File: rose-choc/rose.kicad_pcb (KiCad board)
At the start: 2 copper layers, 145.2 x 97.3 mm, 67 parts, among them SW1 Switch, U1 Arduino_Pro_Micro, U2 TRRS

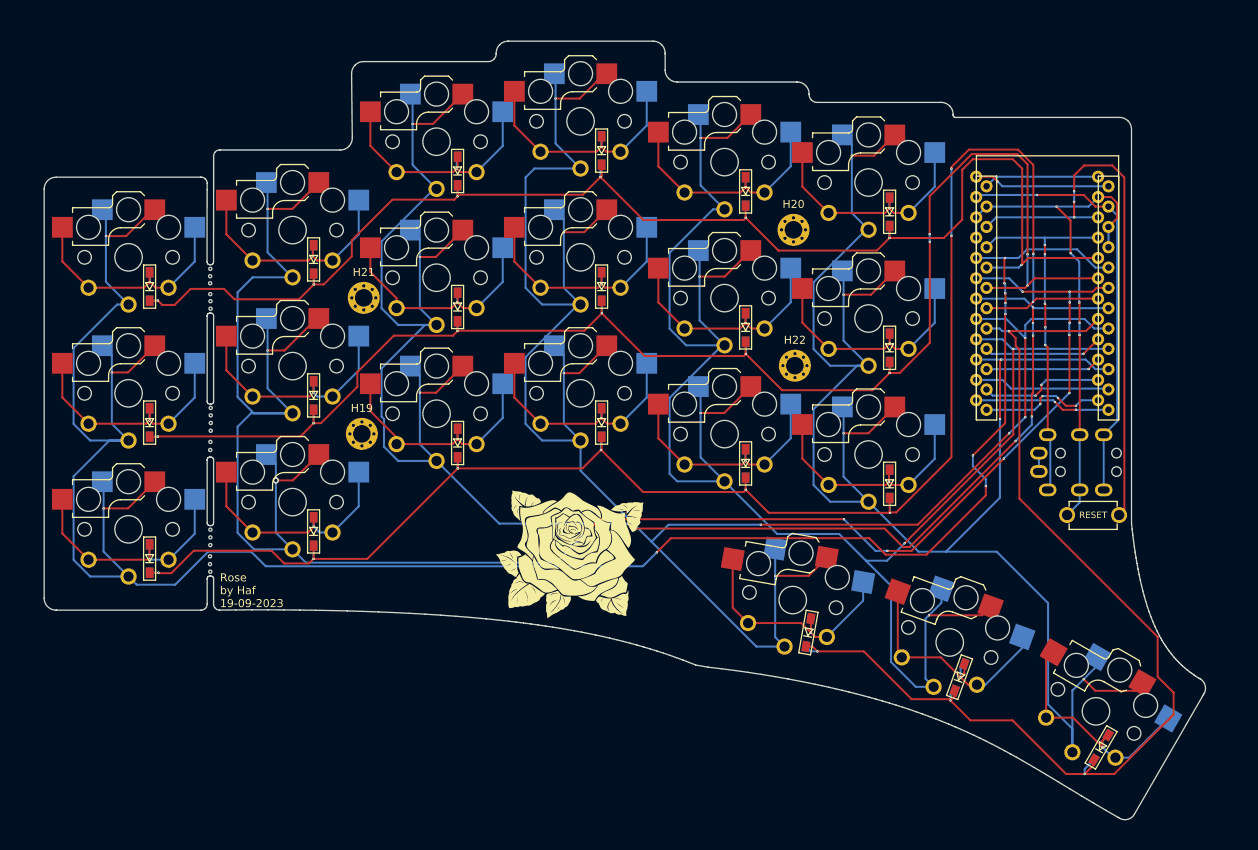
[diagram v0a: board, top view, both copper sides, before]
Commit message: improve tracks and fix vias
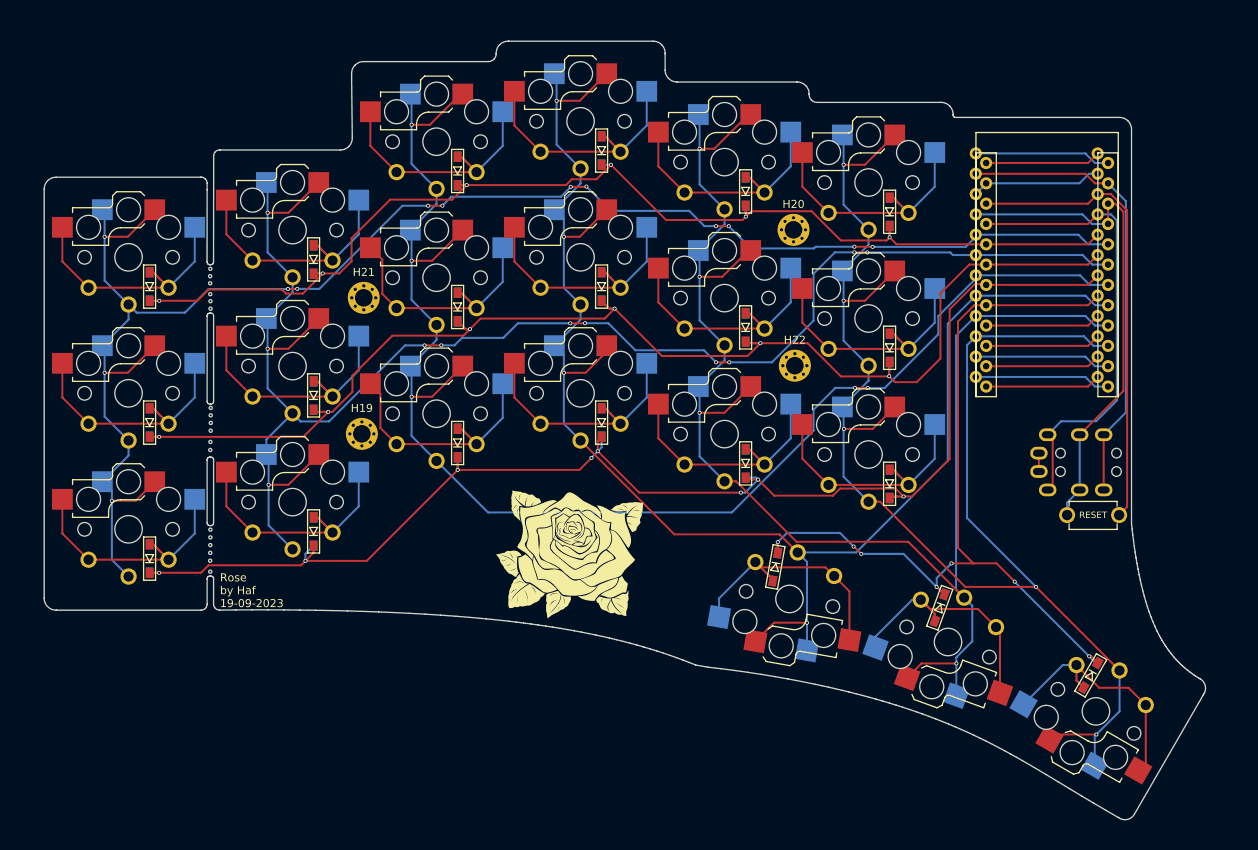
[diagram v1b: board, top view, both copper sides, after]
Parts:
- moved S19 10.2 mm to (132.4, 117.3), turned to 170 degrees
- moved S21 10.2 mm to (172.3, 131.9), turned to 150 degrees
- moved S20 10.1 mm to (153.0, 122.9), turned to 160 degrees
- moved D19 9.19 mm to (129.7, 118.3), turned to -100 degrees
- moved D21 9.09 mm to (169.1, 131.8), turned to -120 degrees
- moved D20 9.02 mm to (150.3, 123.4), turned to -110 degrees
- moved U1 2.91 mm to (163.6, 81.3)
- moved H12 0.43 mm to (59.1, 117.7)
- moved H4 0.43 mm to (59.1, 116.8)
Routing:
- net c1: track 280.4 -> 208.3 mm, vias 11 -> 13
- net c4: track 256.7 -> 190.0 mm, vias 8 -> 4
- net c2: track 259.1 -> 195.6 mm, vias 13 -> 11
- net c3: track 229.9 -> 179.1 mm, vias 9 -> 5
- net c5: track 231.9 -> 186.4 mm, vias 6 -> 4
- net r3: track 211.5 -> 171.8 mm, vias 10 -> 8
- net c6: track 226.5 -> 187.8 mm, vias 6 -> 5
- net r4: track 135.9 -> 107.1 mm, vias 4 -> 7
- net r2: track 190.5 -> 163.4 mm, vias 10 -> 6
- net r1: track 173.5 -> 147.3 mm, vias 7 -> 6
- net GND: track 67.9 -> 81.7 mm, vias 5 -> 0
- net RST: track 69.6 -> 57.5 mm, vias 3 -> 0
- net VCC: track 46.4 -> 57.5 mm, vias 5 -> 0
- net Net-(D14-A): track 30.8 -> 34.1 mm, vias 1 -> 0
- net Net-(D1-A): track 30.8 -> 34.1 mm, vias 1 -> 0
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
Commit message: change diode footprint
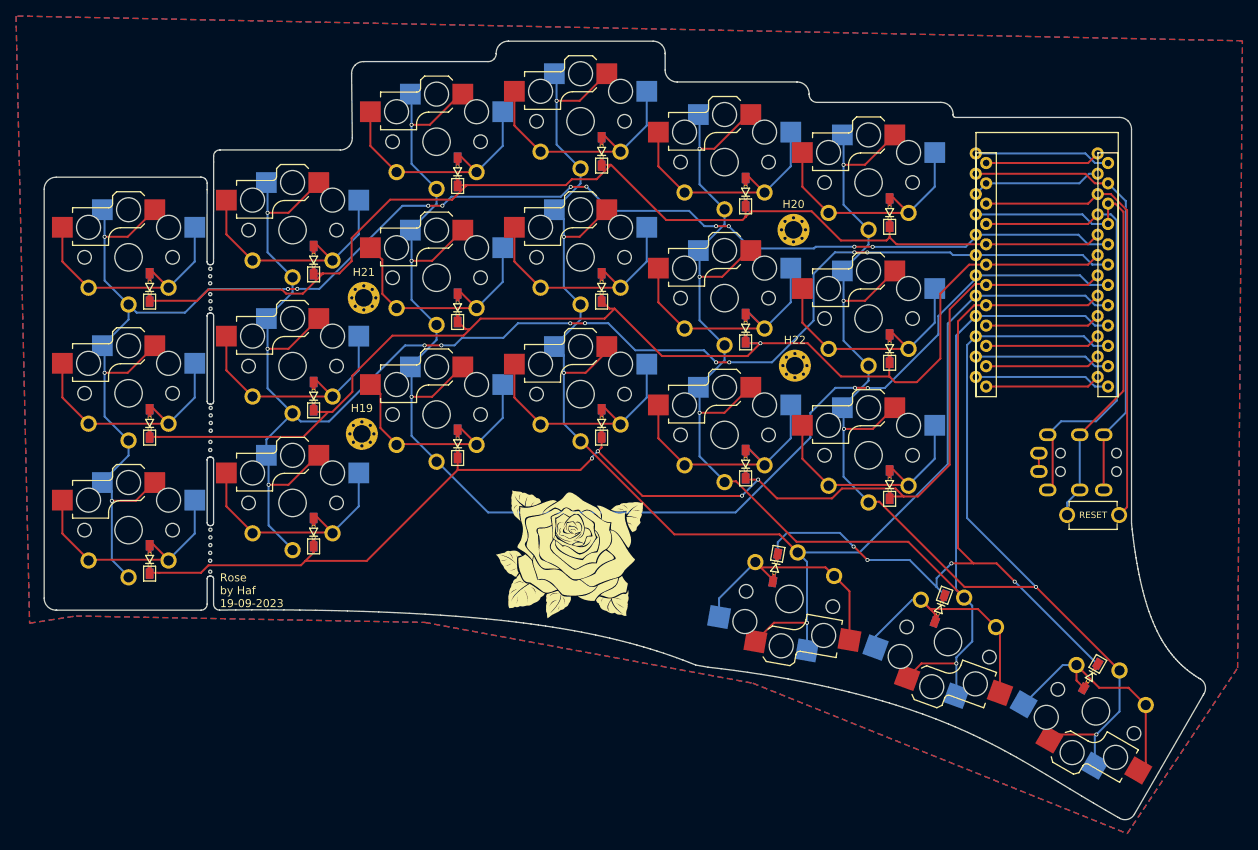
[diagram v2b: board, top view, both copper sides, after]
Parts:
- D1, D10, D11, D12, D13, D14, D15, D16, D17, D18, D19, D2, D20, D21, D3, D4, D5, D6, D7, D8, D9: footprint kbd:D3_SMD -> swoop:D3_SMD
- moved D1 0.10 mm to (51.5, 83.3)
- moved D10 0.10 mm to (108.0, 83.3)
- moved D13 0.10 mm to (51.5, 117.3)
- moved D16 0.10 mm to (108.0, 100.3)
- moved D4 0.10 mm to (108.0, 66.3)
- moved D7 0.10 mm to (51.5, 100.3)
- moved S13 0.10 mm to (48.9, 118.7)
- moved S15 0.10 mm to (87.4, 104.3)
- moved S16 0.10 mm to (105.4, 101.7)
- moved D11 0.10 mm to (126.0, 88.4)
- moved D12 0.10 mm to (144.0, 91.0)
- moved D14 0.10 mm to (72.0, 113.9)
- moved D15 0.10 mm to (90.0, 102.9)
- moved D17 0.10 mm to (126.0, 105.4)
- moved D18 0.10 mm to (144.0, 108.0)
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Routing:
- net r3: track 171.8 -> 162.6 mm, vias 8 -> 4
- net r2: track 163.4 -> 155.0 mm, vias 6 -> 1
- net r1: track 147.3 -> 139.9 mm, vias 6 -> 0
- net r4: track 107.1 -> 102.9 mm, vias 7 -> 4
- net Net-(D20-A): track 35.0 -> 31.6 mm
- net Net-(D21-A): track 34.3 -> 31.1 mm
- net Net-(D9-A): track 34.1 -> 31.0 mm
- net Net-(D8-A): track 34.1 -> 31.0 mm
- net Net-(D6-A): track 34.1 -> 31.0 mm
- net Net-(D3-A): track 34.1 -> 31.0 mm
- net Net-(D2-A): track 34.1 -> 31.0 mm
- net Net-(D18-A): track 34.1 -> 31.0 mm
- net Net-(D12-A): track 34.1 -> 31.0 mm
- net Net-(D5-A): track 34.1 -> 31.0 mm
- net Net-(D15-A): track 34.1 -> 31.0 mm
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- added copper zone on B.Cu, net Net-(D21-A)
- added copper zone on F.Cu, net Net-(D21-A)
